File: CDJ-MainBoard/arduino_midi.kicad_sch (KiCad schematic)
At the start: 22 parts, among them J16 J_JOG, J17 J_PLAY, J18 J_ENCODER_BACK, J19 J_TOUCH, J20 J_LOOP, J21 J_MASTER_TEMPO, J22 J_TEMPO, SW4 RESET_BTN, U14 ATmega32U4-A (Arduino MIDI co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, X1 X322516MLB4SI

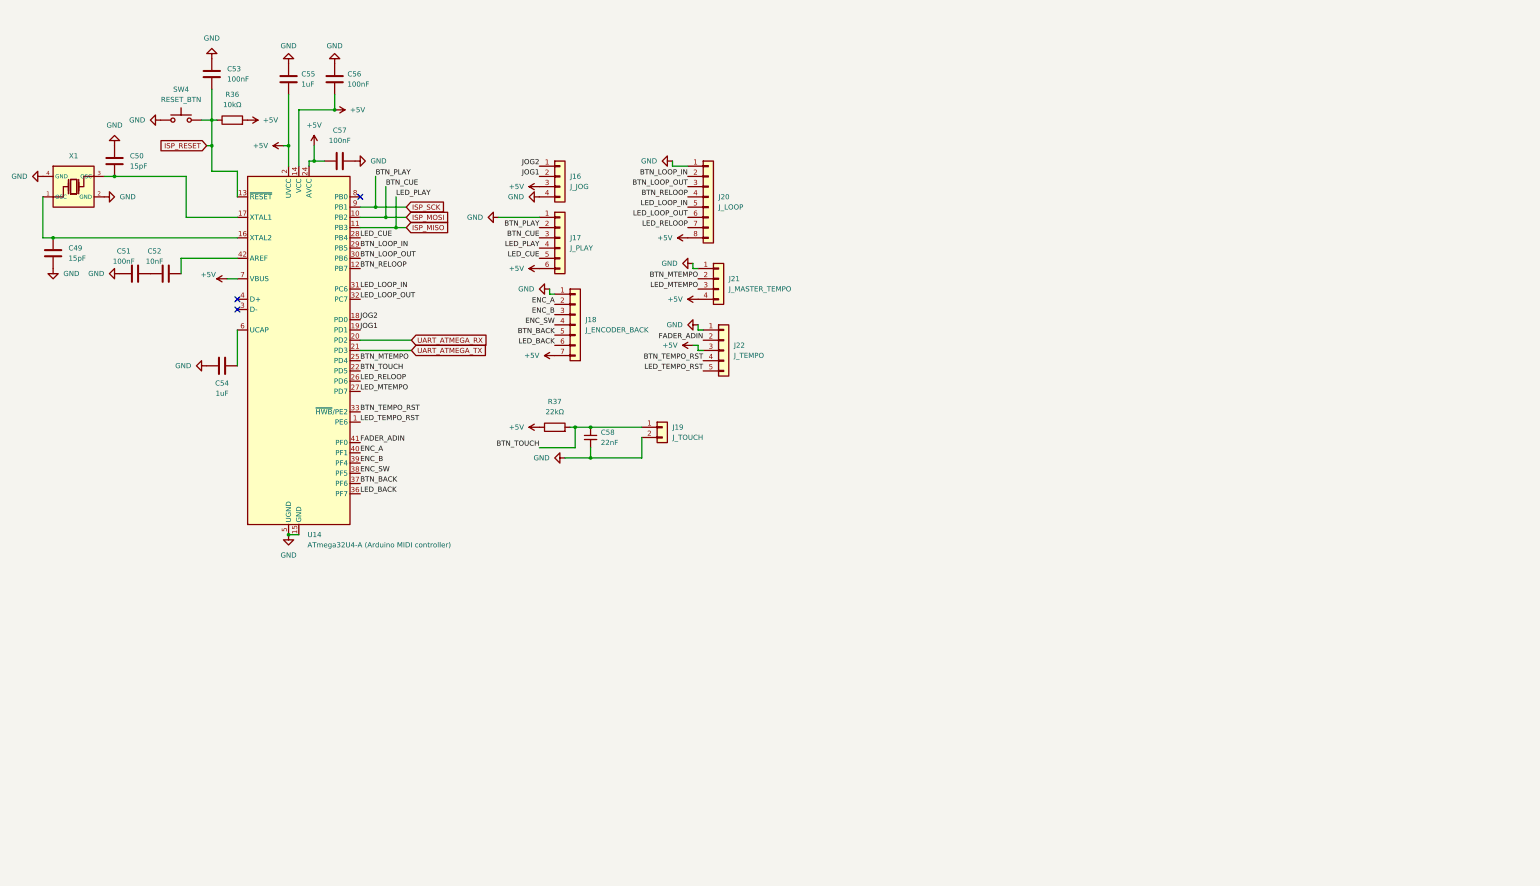
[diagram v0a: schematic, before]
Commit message: Add the simulation sheets for the DAC and buck, add the MCPs multiplexers and the analog ADC multiplexer
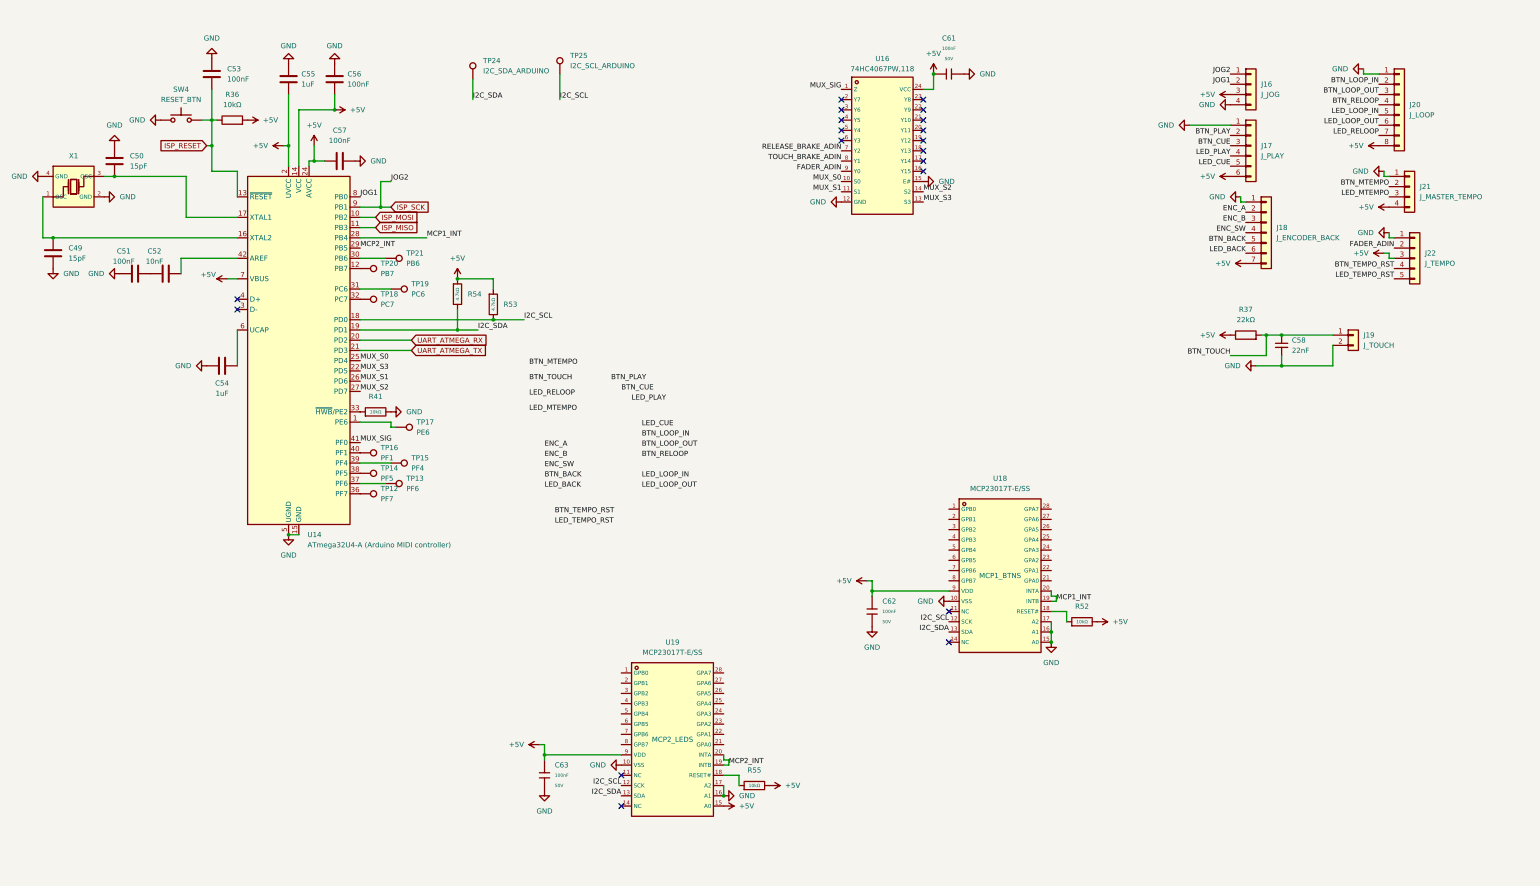
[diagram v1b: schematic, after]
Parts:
- added C61, C62, C63: 100nF, PCM_JLCPCB:C_0402, symbol PCM_JLCPCB-Capacitors:0402,100nF,(2)
- added R41, R52, R55: 10kΩ, PCM_JLCPCB:R_0402, symbol PCM_JLCPCB-Resistors:0402,10kΩ
- added R53, R54: 4.7kΩ, PCM_JLCPCB:R_0402, symbol PCM_JLCPCB-Resistors:0402,4.7kΩ
- added TP12: PF7, symbol Connector:TestPoint
- added TP13: PF6, symbol Connector:TestPoint
- added TP14: PF5, symbol Connector:TestPoint
- added TP15: PF4, symbol Connector:TestPoint
- added TP16: PF1, symbol Connector:TestPoint
- added TP17: PE6, symbol Connector:TestPoint
- added TP18: PC7, symbol Connector:TestPoint
- added TP19: PC6, symbol Connector:TestPoint
- added TP20: PB7, symbol Connector:TestPoint
- added TP21: PB6, symbol Connector:TestPoint
- added TP24: I2C_SDA_ARDUINO, symbol Connector:TestPoint
- added TP25: I2C_SCL_ARDUINO, symbol Connector:TestPoint
- added U16: 74HC4067PW,118, footprint:TSSOP-24_L7.8-W4.4-P0.65-LS6.4-BL, symbol 74HC4067PW,118:74HC4067PW,118
- added U18, U19: MCP23017T-E/SS, footprint:SSOP-28_L10.2-W5.3-P0.65-LS7.8-BL, symbol MCP23017T-E/SS:MCP23017T-E/SS
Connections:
- net +5V: now also C61.1, C62.1, C63.1, R52.2, R53.1, R54.1, R55.2, U16.24 (VCC), U18.9 (VDD), U19.15 (A0), U19.9 (VDD)
- net BTN_BACK: no longer U14.37 (PF6)
- net BTN_LOOP_IN: no longer U14.29 (PB5)
- net BTN_LOOP_OUT: no longer U14.30 (PB6)
- net BTN_MTEMPO: no longer U14.25 (PD4)
- net BTN_RELOOP: no longer U14.12 (PB7)
- net BTN_TEMPO_RST: no longer U14.33 (~{HWB}/PE2)
- net BTN_TOUCH: no longer U14.22 (PD5)
- net ENC_A: no longer U14.40 (PF1)
- net ENC_B: no longer U14.39 (PF4)
- net ENC_SW: no longer U14.38 (PF5)
- net FADER_ADIN: now also U16.9 (Y0); no longer U14.41 (PF0)
- net GND: now also C61.2, C62.2, C63.2, R41.2, U16.12 (GND), U16.15 (E#), U18.10 (VSS), U18.15 (A0), U18.16 (A1), U18.17 (A2), U19.10 (VSS), U19.16 (A1), U19.17 (A2)
- net ISP_MISO: no longer J17.4 (Pin_4)
- net ISP_MOSI: no longer J17.3 (Pin_3)
- net ISP_SCK: now also J16.1 (Pin_1); no longer J17.2 (Pin_2)
- net JOG1: now also U14.8 (PB0); no longer U14.19 (PD1)
- net LED_BACK: no longer U14.36 (PF7)
- net LED_CUE: no longer U14.28 (PB4)
- net LED_LOOP_IN: no longer U14.31 (PC6)
- net LED_LOOP_OUT: no longer U14.32 (PC7)
- net LED_MTEMPO: no longer U14.27 (PD7)
- net LED_RELOOP: no longer U14.26 (PD6)
- net LED_TEMPO_RST: no longer U14.1 (PE6)
- net JOG2 renamed I2C_SCL
- net I2C_SCL: now also R53.2, TP25.1, U18.12 (SCK), U19.12 (SCK); no longer J16.1 (Pin_1)
- new net: TP12.1, U14.36 (PF7)
- new net: TP15.1, U14.39 (PF4)
- new net: TP19.1, U14.31 (PC6)
- new net: R41.1, U14.33 (~{HWB}/PE2)
- new net: R52.1, U18.18 (RESET#)
- new net: TP20.1, U14.12 (PB7)
- new net: TP18.1, U14.32 (PC7)
- new net: TP17.1, U14.1 (PE6)
- new net: TP21.1, U14.30 (PB6)
- new net: TP13.1, U14.37 (PF6)
- new net: TP14.1, U14.38 (PF5)
- new net: TP16.1, U14.40 (PF1)
- new net: R55.1, U19.18 (RESET#)
- new net BTN_CUE: J17.3 (Pin_3)
- new net BTN_PLAY: J17.2 (Pin_2)
- new net I2C_SDA: R54.2, TP24.1, U14.19 (PD1), U18.13 (SDA), U19.13 (SDA)
- new net LED_PLAY: J17.4 (Pin_4)
- new net MCP1_INT: U14.28 (PB4), U18.19 (INTB), U18.20 (INTA)
- new net MCP2_INT: U14.29 (PB5), U19.19 (INTB), U19.20 (INTA)
- new net MUX_S0: U14.25 (PD4), U16.10 (S0)
- new net MUX_S1: U14.26 (PD6), U16.11 (S1)
- new net MUX_S2: U14.27 (PD7), U16.14 (S2)
- new net MUX_S3: U14.22 (PD5), U16.13 (S3)
- new net MUX_SIG: U14.41 (PF0), U16.1 (Z)
- new net RELEASE_BRAKE_ADIN: U16.7 (Y2)
- new net TOUCH_BRAKE_ADIN: U16.8 (Y1)
- no-connect marks 3 -> 19
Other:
- title: (none) -> Arduino MIDI IO part with muxers
- moved on the sheet: C58, J16, J17, J18, J19, J20, J21, J22, R37

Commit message: Add connectors for sections of inputs, and list of all inputs in XLSX
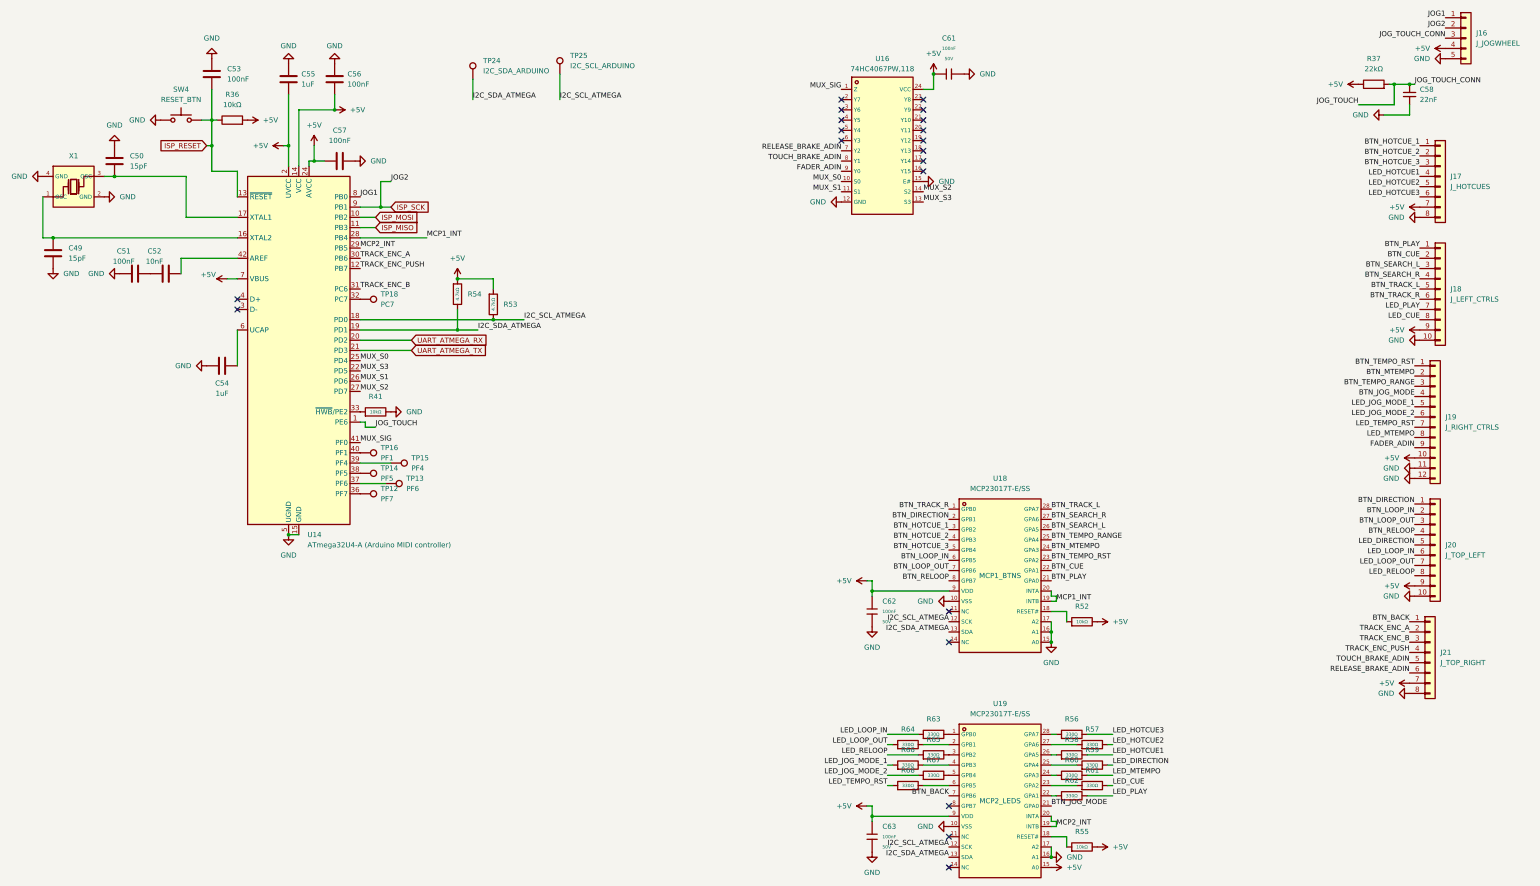
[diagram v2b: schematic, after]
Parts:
- removed J16: J_JOG, Connector_JST:JST_PH_B4B-PH-K_1x04_P2.00mm_Vertical, symbol Connector_Generic:Conn_01x04
- removed J17: J_PLAY, Connector_JST:JST_PH_B6B-PH-K_1x06_P2.00mm_Vertical, symbol Connector_Generic:Conn_01x06
- removed J18: J_ENCODER_BACK, Connector_JST:JST_PH_B7B-PH-K_1x07_P2.00mm_Vertical, symbol Connector_Generic:Conn_01x07
- removed J19: J_TOUCH, Connector_JST:JST_PH_B2B-PH-K_1x02_P2.00mm_Vertical, symbol Connector_Generic:Conn_01x02
- removed J20: J_LOOP, Connector_JST:JST_PH_B8B-PH-K_1x08_P2.00mm_Vertical, symbol Connector_Generic:Conn_01x08
- removed J21: J_MASTER_TEMPO, Connector_JST:JST_PH_B4B-PH-K_1x04_P2.00mm_Vertical, symbol Connector_Generic:Conn_01x04
- removed J22: J_TEMPO, Connector_JST:JST_PH_B5B-PH-K_1x05_P2.00mm_Vertical, symbol Connector_Generic:Conn_01x05
- removed TP17: PE6, symbol Connector:TestPoint
- removed TP19: PC6, symbol Connector:TestPoint
- removed TP20: PB7, symbol Connector:TestPoint
- removed TP21: PB6, symbol Connector:TestPoint
- added J16: J_JOGWHEEL, Connector_JST:JST_PH_B5B-PH-K_1x05_P2.00mm_Vertical, symbol Connector_Generic:Conn_01x05
- added J17: J_HOTCUES, Connector_JST:JST_PH_B8B-PH-K_1x08_P2.00mm_Vertical, symbol Connector_Generic:Conn_01x08
- added J18: J_LEFT_CTRLS, Connector_JST:JST_PH_B10B-PH-K_1x10_P2.00mm_Vertical, symbol Connector_Generic:Conn_01x10
- added J19: J_RIGHT_CTRLS, Connector_JST:JST_PH_B12B-PH-K_1x12_P2.00mm_Vertical, symbol Connector_Generic:Conn_01x12
- added J20: J_TOP_LEFT, Connector_JST:JST_PH_B10B-PH-K_1x10_P2.00mm_Vertical, symbol Connector_Generic:Conn_01x10
- added J21: J_TOP_RIGHT, Connector_JST:JST_PH_B8B-PH-K_1x08_P2.00mm_Vertical, symbol Connector_Generic:Conn_01x08
- added R56, R57, R58, R59, R60, R61, R62, R63, R64, R65, R66, R67, R68: 330Ω, PCM_JLCPCB:R_0402, symbol PCM_JLCPCB-Resistors:0402,330Ω
- TP12, TP13, TP14, TP15, TP16, TP18: footprint (none) -> TestPoint:TestPoint_Pad_2.0x2.0mm
- TP24, TP25: footprint (none) -> TestPoint:TestPoint_Pad_1.5x1.5mm
- U16: footprint footprint:TSSOP-24_L7.8-W4.4-P0.65-LS6.4-BL -> JLC2KiCad_lib-footprints:TSSOP-28_L9.8-W6.6-P0.65-BL
- U18, U19: footprint footprint:SSOP-28_L10.2-W5.3-P0.65-LS7.8-BL -> JLC2KiCad_lib-footprints:SSOP-28_L10.2-W5.3-P0.65-LS7.8-BL
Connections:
- net BTN_TOUCH is gone; now on net JOG_TOUCH: C58.1, R37.2
- net +5V: now also J16.4 (Pin_4), J17.7 (Pin_7), J18.9 (Pin_9), J19.10 (Pin_10), J20.9 (Pin_9), J21.7 (Pin_7)
- net BTN_BACK: now also U19.7 (GPB6), J21.1 (Pin_1)
- net BTN_CUE: now also U18.22 (GPA1), J18.2 (Pin_2)
- net BTN_LOOP_IN: now also U18.6 (GPB5), J20.2 (Pin_2)
- net BTN_LOOP_OUT: now also U18.7 (GPB6), J20.3 (Pin_3)
- net BTN_MTEMPO: now also U18.24 (GPA3), J19.2 (Pin_2)
- net BTN_PLAY: now also U18.21 (GPA0), J18.1 (Pin_1)
- net BTN_RELOOP: now also U18.8 (GPB7), J20.4 (Pin_4)
- net BTN_TEMPO_RST: now also U18.23 (GPA2), J19.1 (Pin_1)
- net FADER_ADIN: now also J19.9 (Pin_9)
- net GND: now also J16.5 (Pin_5), J17.8 (Pin_8), J18.10 (Pin_10), J19.11 (Pin_11), J19.12 (Pin_12), J20.10 (Pin_10), J21.8 (Pin_8)
- net ISP_SCK: now also J16.2 (Pin_2)
- net JOG1: now also J16.1 (Pin_1)
- net LED_CUE: now also J18.8 (Pin_8), R61.2
- net LED_LOOP_IN: now also J20.6 (Pin_6), R63.1
- net LED_LOOP_OUT: now also J20.7 (Pin_7), R64.1
- net LED_MTEMPO: now also J19.8 (Pin_8), R60.2
- net LED_PLAY: now also J18.7 (Pin_7), R62.2
- net LED_RELOOP: now also J20.8 (Pin_8), R65.1
- net LED_TEMPO_RST: now also J19.7 (Pin_7), R68.1
- net RELEASE_BRAKE_ADIN: now also J21.6 (Pin_6)
- net TOUCH_BRAKE_ADIN: now also J21.5 (Pin_5)
- net TRACK_ENC_B: now reaches U14.31 (PC6)
- net TRACK_ENC_B: now also J21.3 (Pin_3)
- net TRACK_ENC_PUSH: now reaches U14.12 (PB7)
- net TRACK_ENC_PUSH: now also J21.4 (Pin_4)
- net JOG_TOUCH: now reaches U14.1 (PE6)
- net JOG_TOUCH: now also J16.3 (Pin_3)
- net TRACK_ENC_A: now reaches U14.30 (PB6)
- net TRACK_ENC_A: now also J21.2 (Pin_2)
- net BTN_TRACK_R: now reaches U18.1 (GPB0)
- net BTN_TRACK_R: now also J18.6 (Pin_6)
- net BTN_DIRECTION: now reaches U18.2 (GPB1)
- net BTN_DIRECTION: now also J20.1 (Pin_1)
- net BTN_TEMPO_RANGE: now reaches U18.25 (GPA4)
- net BTN_TEMPO_RANGE: now also J19.3 (Pin_3)
- net BTN_SEARCH_L: now reaches U18.26 (GPA5)
- net BTN_SEARCH_L: now also J18.3 (Pin_3)
- net BTN_SEARCH_R: now reaches U18.27 (GPA6)
- net BTN_SEARCH_R: now also J18.4 (Pin_4)
- net BTN_TRACK_L: now reaches U18.28 (GPA7)
- net BTN_TRACK_L: now also J18.5 (Pin_5)
- net BTN_HOTCUE_1: now reaches U18.3 (GPB2)
- net BTN_HOTCUE_1: now also J17.1 (Pin_1)
- net BTN_HOTCUE_2: now reaches U18.4 (GPB3)
- net BTN_HOTCUE_2: now also J17.2 (Pin_2)
- net BTN_HOTCUE_3: now reaches U18.5 (GPB4)
- net BTN_HOTCUE_3: now also J17.3 (Pin_3)
- net at U19.1 (GPB0): now also R63.2
- net at U19.2 (GPB1): now also R64.2
- net BTN_JOG_MODE: now reaches U19.21 (GPA0)
- net BTN_JOG_MODE: now also J19.4 (Pin_4)
- net at U19.22 (GPA1): now also R62.1
- net at U19.23 (GPA2): now also R61.1
- net at U19.24 (GPA3): now also R60.1
- net at U19.25 (GPA4): now also R59.1
- net at U19.26 (GPA5): now also R58.1
- net at U19.27 (GPA6): now also R57.1
- net at U19.28 (GPA7): now also R56.1
- net at U19.3 (GPB2): now also R65.2
- net at U19.4 (GPB3): now also R66.2
- net at U19.5 (GPB4): now also R67.2
- net at U19.6 (GPB5): now also R68.2
- net I2C_SCL renamed I2C_SCL_ATMEGA
- net I2C_SDA renamed I2C_SDA_ATMEGA
- new net LED_DIRECTION: J20.5 (Pin_5), R59.2
- new net LED_HOTCUE1: J17.4 (Pin_4), R58.2
- new net LED_HOTCUE2: J17.5 (Pin_5), R57.2
- new net LED_HOTCUE3: J17.6 (Pin_6), R56.2
- new net LED_JOG_MODE_1: J19.5 (Pin_5), R66.1
- new net LED_JOG_MODE_2: J19.6 (Pin_6), R67.1
- no-connect marks 19 -> 20
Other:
- moved on the sheet: C58, C63, R37, R55, U19

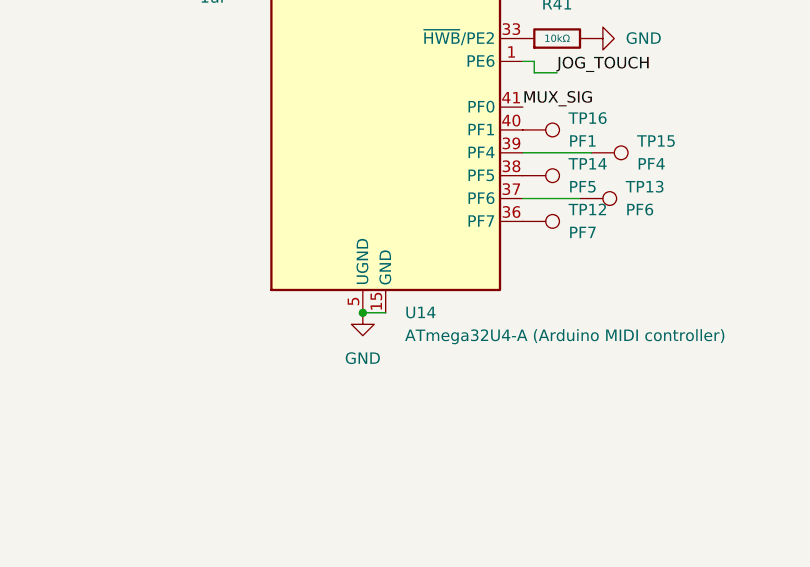
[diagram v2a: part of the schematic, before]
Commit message: Route the audio and arduino itself, fix 3.3V bus
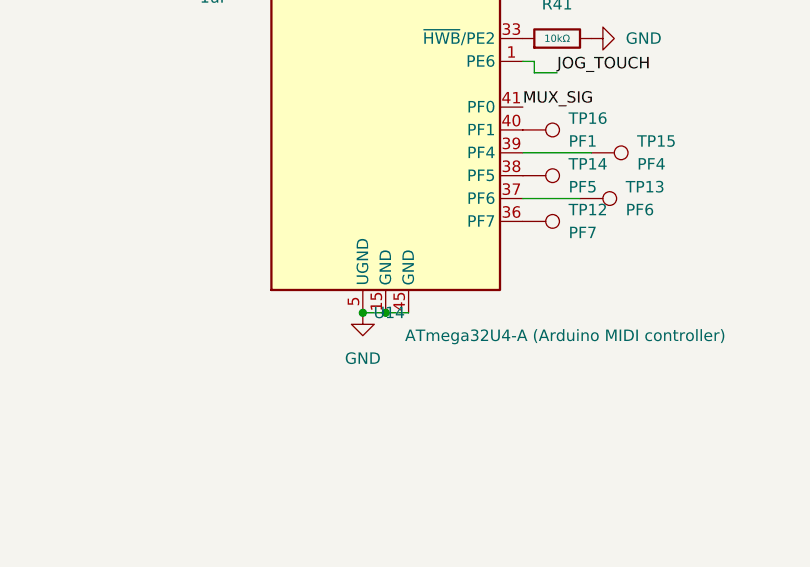
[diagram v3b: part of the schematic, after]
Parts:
- U14: footprint JLC2KiCad_lib-footprints:VQFN-44_L7.0-W7.0-P0.50-BL-EP5.2 -> Package_QFP:TQFP-44_10x10mm_P0.8mm
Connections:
- net GND: now also U14.45 (GND)
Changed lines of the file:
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@@
 	)
 	(junction
+		(at 100.33 147.32)
+		(diameter 0)
+		(color 0 0 0 0)
+	)
+	(junction
 		(at 287.02 173.99)
 		(diameter 0)
@@
 	(wire
 		(pts
+			(xy 100.33 147.32) (xy 102.87 147.32)
+		)
+		(stroke
+			(width 0)
+			(type default)
+		)
+	)
+	(wire
+		(pts
 			(xy 52.07 58.42) (xy 54.61 58.42)
 		)
@@
 		(on_board yes)
 		(dnp no)
-		(fields_autoplaced yes)
 		(property "Reference" "U14"
 			(at 102.4733 147.32 0)
@@
 					(size 1.27 1.27)
 				)
-				(justify left)
+				(justify right)
 			)
 		)
@@
 			)
 		)
-		(property "Footprint" "JLC2KiCad_lib-footprints:VQFN-44_L7.0-W7.0-P0.50-BL-EP5.2"
+		(property "Footprint" "Package_QFP:TQFP-44_10x10mm_P0.8mm"
 			(at 100.33 101.6 0)
 			(effects
@@
 		(pin "11"
 		)
+		(pin "45"
+		)
 		(instances
